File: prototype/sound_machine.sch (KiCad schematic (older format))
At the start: 18 parts, among them J1 Conn_01x04, J10 Conn_01x01, J11 Conn_01x01, J12 Conn_01x01, J13 Conn_01x15, J16 Conn_01x15, J2 Conn_01x15, J3 Conn_01x15, J4 Conn_01x08, J5 Audio-Jack-3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

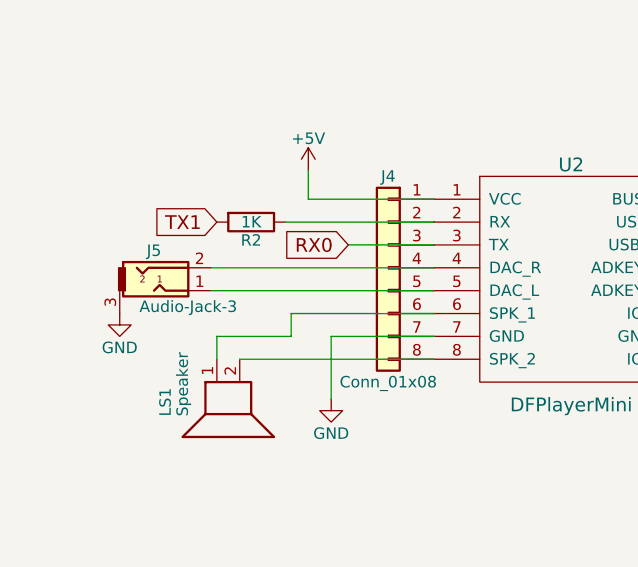
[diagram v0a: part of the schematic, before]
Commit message: Removed jack
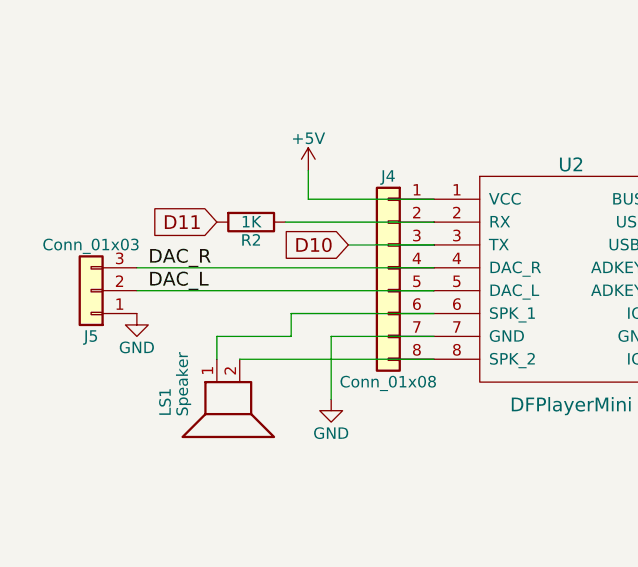
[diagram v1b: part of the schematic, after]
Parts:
- removed J5: Audio-Jack-3, Connectors:BARREL_JACK, symbol Audio-Jack-3
- added J5: Conn_01x03, Pin_Headers:Pin_Header_Straight_1x03_Pitch2.54mm, symbol Conn_01x03
- R1: footprint Resistors_SMD:R_0805_HandSoldering -> Resistors_THT:R_Axial_DIN0207_L6.3mm_D2.5mm_P10.16mm_Horizontal
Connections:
- net D10: now also J4.3 (Pin_3), U2.3 (TX)
- net D11: now also R2.2
- net GND: now also J5.1 (Pin_1)
- net RX0: no longer J4.3 (Pin_3), U2.3 (TX)
- net TX1: no longer R2.2
- net DAC_R: now reaches J4.4 (Pin_4), U2.4 (DAC_R)
- net DAC_R: now also J5.3 (Pin_3)
- net DAC_L: now reaches J4.5 (Pin_5), U2.5 (DAC_L)
- net DAC_L: now also J5.2 (Pin_2)
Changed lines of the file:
@@
 F 0 "R1" V 8430 2900 50  0000 C CNN
 F 1 "330R" V 8350 2900 50  0000 C CNN
-F 2 "Resistors_SMD:R_0805_HandSoldering" V 8280 2900 50  0001 C CNN
+F 2 "Resistors_THT:R_Axial_DIN0207_L6.3mm_D2.5mm_P10.16mm_Horizontal" V 8280 2900 50  0001 C CNN
 F 3 "" H 8350 2900 50  0001 C CNN
 	1    8350 2900
@@
 NoConn ~ 8500 2800
 $Comp
-L Audio-Jack-3 J5
-U 1 1 5A3D91A5
-P 2625 4575
-F 0 "J5" H 2575 4750 50  0000 C CNN
-F 1 "Audio-Jack-3" H 2725 4505 50  0000 C CNN
-F 2 "Connectors:BARREL_JACK" H 2875 4675 50  0001 C CNN
-F 3 "" H 2875 4675 50  0001 C CNN
-	1    2625 4575
-	1    0    0    -1
-$EndComp
-$Comp
 L GND #PWR010
 U 1 1 5A3D91F2
-P 2425 4675
-F 0 "#PWR010" H 2425 4425 50  0001 C CNN
-F 1 "GND" H 2425 4525 50  0000 C CNN
-F 2 "" H 2425 4675 50  0001 C CNN
-F 3 "" H 2425 4675 50  0001 C CNN
-	1    2425 4675
-	1    0    0    -1
-$EndComp
-Text GLabel 2850 4275 0    60   Input ~ 0
-TX1
-Text GLabel 3425 4375 0    60   Input ~ 0
-RX0
+P 2500 4675
+F 0 "#PWR010" H 2500 4425 50  0001 C CNN
+F 1 "GND" H 2500 4525 50  0000 C CNN
+F 2 "" H 2500 4675 50  0001 C CNN
+F 3 "" H 2500 4675 50  0001 C CNN
+	1    2500 4675
+	1    0    0    -1
+$EndComp
 $Comp
 L R R2
@@
 	2850 4775 2850 4875
 Wire Wire Line
-	2825 4575 3800 4575
-Wire Wire Line
-	2825 4475 3800 4475
+	2500 4575 3800 4575
+Wire Wire Line
+	2500 4475 3800 4475
 Wire Wire Line
 	3150 4275 3800 4275
@@
 	1    0    0    -1
 $EndComp
+Text GLabel 3425 4375 0    60   Input ~ 0
+D10
+Text GLabel 2850 4275 0    60   Input ~ 0
+D11
+$Comp
+L Conn_01x03 J5
+U 1 1 5A438329
+P 2300 4575
+F 0 "J5" H 2300 4775 50  0000 C CNN
+F 1 "Conn_01x03" H 2300 4375 50  0000 C CNN
+F 2 "Pin_Headers:Pin_Header_Straight_1x03_Pitch2.54mm" H 2300 4575 50  0001 C CNN
+F 3 "" H 2300 4575 50  0001 C CNN
+	1    2300 4575
+	-1   0    0    1
+$EndComp
+Text Label 2550 4475 0    60   ~ 0
+DAC_R
+Text Label 2550 4575 0    60   ~ 0
+DAC_L
 $EndSCHEMATC

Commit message: Capacitor
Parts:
- added C1: 10uf, Capacitors_THT:CP_Radial_D5.0mm_P2.50mm, symbol CP
- J1: footprint Pin_Headers:Pin_Header_Straight_1x04_Pitch2.54mm -> Socket_Strips:Socket_Strip_Straight_1x04
- J13, J16: footprint Pin_Headers:Pin_Header_Straight_1x15_Pitch2.54mm -> Socket_Strips:Socket_Strip_Straight_1x15_Pitch2.54mm
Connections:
- net +5V: now also C1.1
- net GND: now also C1.2
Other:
- moved on the sheet: J16, J3
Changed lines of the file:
@@
 L Conn_01x15 J3
 U 1 1 5A3D80E6
-P 4275 2350
-F 0 "J3" H 4275 3150 50  0000 C CNN
-F 1 "Conn_01x15" H 4275 1550 50  0000 C CNN
-F 2 "Pin_Headers:Pin_Header_Straight_1x15_Pitch2.54mm" H 4275 2350 50  0001 C CNN
-F 3 "" H 4275 2350 50  0001 C CNN
-	1    4275 2350
+P 5425 2375
+F 0 "J3" H 5425 3175 50  0000 C CNN
+F 1 "Conn_01x15" H 5425 1575 50  0000 C CNN
+F 2 "Pin_Headers:Pin_Header_Straight_1x15_Pitch2.54mm" H 5425 2375 50  0001 C CNN
+F 3 "" H 5425 2375 50  0001 C CNN
+	1    5425 2375
 	-1   0    0    -1
 $EndComp
-Text GLabel 4475 1650 2    60   Input ~ 0
+Text GLabel 5625 1675 2    60   Input ~ 0
 VIN
-Text GLabel 4475 1850 2    60   Input ~ 0
+Text GLabel 5625 1875 2    60   Input ~ 0
 RESET
-Text GLabel 4475 2050 2    60   Input ~ 0
+Text GLabel 5625 2075 2    60   Input ~ 0
 A7
-Text GLabel 4475 2150 2    60   Input ~ 0
+Text GLabel 5625 2175 2    60   Input ~ 0
 A6
-Text GLabel 4475 2450 2    60   Input ~ 0
+Text GLabel 5625 2475 2    60   Input ~ 0
 A3
-Text GLabel 4475 2550 2    60   Input ~ 0
+Text GLabel 5625 2575 2    60   Input ~ 0
 A2
-Text GLabel 4475 2650 2    60   Input ~ 0
+Text GLabel 5625 2675 2    60   Input ~ 0
 A1
-Text GLabel 4475 2750 2    60   Input ~ 0
+Text GLabel 5625 2775 2    60   Input ~ 0
 A0
-Text GLabel 4475 2850 2    60   Input ~ 0
+Text GLabel 5625 2875 2    60   Input ~ 0
 AHREF
-Text GLabel 4475 3050 2    60   Input ~ 0
+Text GLabel 5625 3075 2    60   Input ~ 0
 D13
 $Comp
 L +3.3V #PWR07
 U 1 1 5A3D8305
-P 5025 2950
-F 0 "#PWR07" H 5025 2800 50  0001 C CNN
-F 1 "+3.3V" H 5025 3090 50  0000 C CNN
-F 2 "" H 5025 2950 50  0001 C CNN
-F 3 "" H 5025 2950 50  0001 C CNN
-	1    5025 2950
+P 6175 2975
+F 0 "#PWR07" H 6175 2825 50  0001 C CNN
+F 1 "+3.3V" H 6175 3115 50  0000 C CNN
+F 2 "" H 6175 2975 50  0001 C CNN
+F 3 "" H 6175 2975 50  0001 C CNN
+	1    6175 2975
 	1    0    0    -1
 $EndComp
@@
 L +5V #PWR08
 U 1 1 5A3D8374
-P 5000 1950
-F 0 "#PWR08" H 5000 1800 50  0001 C CNN
-F 1 "+5V" H 5000 2090 50  0000 C CNN
-F 2 "" H 5000 1950 50  0001 C CNN
-F 3 "" H 5000 1950 50  0001 C CNN
-	1    5000 1950
+P 6150 1975
+F 0 "#PWR08" H 6150 1825 50  0001 C CNN
+F 1 "+5V" H 6150 2115 50  0000 C CNN
+F 2 "" H 6150 1975 50  0001 C CNN
+F 3 "" H 6150 1975 50  0001 C CNN
+	1    6150 1975
 	1    0    0    -1
 $EndComp
@@
 L GND #PWR09
 U 1 1 5A3D83F0
-P 5200 1750
-F 0 "#PWR09" H 5200 1500 50  0001 C CNN
-F 1 "GND" H 5200 1600 50  0000 C CNN
-F 2 "" H 5200 1750 50  0001 C CNN
-F 3 "" H 5200 1750 50  0001 C CNN
-	1    5200 1750
-	1    0    0    -1
-$EndComp
-Text GLabel 4475 2250 2    60   Input ~ 0
+P 6350 1775
+F 0 "#PWR09" H 6350 1525 50  0001 C CNN
+F 1 "GND" H 6350 1625 50  0000 C CNN
+F 2 "" H 6350 1775 50  0001 C CNN
+F 3 "" H 6350 1775 50  0001 C CNN
+	1    6350 1775
+	1    0    0    -1
+$EndComp
+Text GLabel 5625 2275 2    60   Input ~ 0
 SCL
-Text GLabel 4475 2350 2    60   Input ~ 0
+Text GLabel 5625 2375 2    60   Input ~ 0
 SDA
 Text GLabel 8200 2900 0    60   Input ~ 0
@@
 	2075 1975 2425 1975
 Wire Wire Line
-	5025 2950 4475 2950
-Wire Wire Line
-	5000 1950 4475 1950
-Wire Wire Line
-	4475 1750 5200 1750
+	6175 2975 5625 2975
+Wire Wire Line
+	6150 1975 5625 1975
+Wire Wire Line
+	5625 1775 6350 1775
 Wire Wire Line
 	2950 4875 3800 4875
@@
 F 0 "J13" H 3375 3175 50  0000 C CNN
 F 1 "Conn_01x15" H 3375 1575 50  0000 C CNN
-F 2 "Pin_Headers:Pin_Header_Straight_1x15_Pitch2.54mm" H 3375 2375 50  0001 C CNN
+F 2 "Socket_Strips:Socket_Strip_Straight_1x15_Pitch2.54mm" H 3375 2375 50  0001 C CNN
 F 3 "" H 3375 2375 50  0001 C CNN
 	1    3375 2375
@@
 L Conn_01x15 J16
 U 1 1 5A3DC180
-P 5400 2350
-F 0 "J16" H 5400 3150 50  0000 C CNN
-F 1 "Conn_01x15" H 5400 1550 50  0000 C CNN
-F 2 "Pin_Headers:Pin_Header_Straight_1x15_Pitch2.54mm" H 5400 2350 50  0001 C CNN
-F 3 "" H 5400 2350 50  0001 C CNN
-	1    5400 2350
+P 4250 2375
+F 0 "J16" H 4250 3175 50  0000 C CNN
+F 1 "Conn_01x15" H 4250 1575 50  0000 C CNN
+F 2 "Socket_Strips:Socket_Strip_Straight_1x15_Pitch2.54mm" H 4250 2375 50  0001 C CNN
+F 3 "" H 4250 2375 50  0001 C CNN
+	1    4250 2375
 	-1   0    0    -1
 $EndComp
-Text GLabel 5600 1650 2    60   Input ~ 0
+Text GLabel 4450 1675 2    60   Input ~ 0
 VIN
-Text GLabel 5600 1850 2    60   Input ~ 0
+Text GLabel 4450 1875 2    60   Input ~ 0
 RESET
-Text GLabel 5600 2050 2    60   Input ~ 0
+Text GLabel 4450 2075 2    60   Input ~ 0
 A7
-Text GLabel 5600 2150 2    60   Input ~ 0
+Text GLabel 4450 2175 2    60   Input ~ 0
 A6
-Text GLabel 5600 2450 2    60   Input ~ 0
+Text GLabel 4450 2475 2    60   Input ~ 0
 A3
-Text GLabel 5600 2550 2    60   Input ~ 0
+Text GLabel 4450 2575 2    60   Input ~ 0
 A2
-Text GLabel 5600 2650 2    60   Input ~ 0
+Text GLabel 4450 2675 2    60   Input ~ 0
 A1
-Text GLabel 5600 2750 2    60   Input ~ 0
+Text GLabel 4450 2775 2    60   Input ~ 0
 A0
-Text GLabel 5600 2850 2    60   Input ~ 0
+Text GLabel 4450 2875 2    60   Input ~ 0
 AHREF
-Text GLabel 5600 3050 2    60   Input ~ 0
+Text GLabel 4450 3075 2    60   Input ~ 0
 D13
 $Comp
 L +3.3V #PWR017
 U 1 1 5A3DC190
-P 6150 2950
-F 0 "#PWR017" H 6150 2800 50  0001 C CNN
-F 1 "+3.3V" H 6150 3090 50  0000 C CNN
-F 2 "" H 6150 2950 50  0001 C CNN
-F 3 "" H 6150 2950 50  0001 C CNN
-	1    6150 2950
+P 5000 2975
+F 0 "#PWR017" H 5000 2825 50  0001 C CNN
+F 1 "+3.3V" H 5000 3115 50  0000 C CNN
+F 2 "" H 5000 2975 50  0001 C CNN
+F 3 "" H 5000 2975 50  0001 C CNN
+	1    5000 2975
 	1    0    0    -1
 $EndComp
@@
 L +5V #PWR018
 U 1 1 5A3DC196
-P 6125 1950
-F 0 "#PWR018" H 6125 1800 50  0001 C CNN
-F 1 "+5V" H 6125 2090 50  0000 C CNN
-F 2 "" H 6125 1950 50  0001 C CNN
-F 3 "" H 6125 1950 50  0001 C CNN
-	1    6125 1950
+P 4975 1975
+F 0 "#PWR018" H 4975 1825 50  0001 C CNN
+F 1 "+5V" H 4975 2115 50  0000 C CNN
+F 2 "" H 4975 1975 50  0001 C CNN
+F 3 "" H 4975 1975 50  0001 C CNN
+	1    4975 1975
 	1    0    0    -1
 $EndComp
@@
 L GND #PWR019
 U 1 1 5A3DC19C
-P 6325 1750
-F 0 "#PWR019" H 6325 1500 50  0001 C CNN
-F 1 "GND" H 6325 1600 50  0000 C CNN
-F 2 "" H 6325 1750 50  0001 C CNN
-F 3 "" H 6325 1750 50  0001 C CNN
-	1    6325 1750
-	1    0    0    -1
-$EndComp
-Text GLabel 5600 2250 2    60   Input ~ 0
+P 5175 1775
+F 0 "#PWR019" H 5175 1525 50  0001 C CNN
+F 1 "GND" H 5175 1625 50  0000 C CNN
+F 2 "" H 5175 1775 50  0001 C CNN
+F 3 "" H 5175 1775 50  0001 C CNN
+	1    5175 1775
+	1    0    0    -1
+$EndComp
+Text GLabel 4450 2275 2    60   Input ~ 0
 SCL
-Text GLabel 5600 2350 2    60   Input ~ 0
+Text GLabel 4450 2375 2    60   Input ~ 0
 SDA
 Wire Wire Line
-	6150 2950 5600 2950
-Wire Wire Line
-	6125 1950 5600 1950
-Wire Wire Line
-	5600 1750 6325 1750
+	5000 2975 4450 2975
+Wire Wire Line
+	4975 1975 4450 1975
+Wire Wire Line
+	4450 1775 5175 1775
 $Comp
 L Conn_01x08 J6
@@
 F 0 "J1" H 9175 5400 50  0000 C CNN
 F 1 "Conn_01x04" H 9175 4900 50  0000 C CNN
-F 2 "Pin_Headers:Pin_Header_Straight_1x04_Pitch2.54mm" H 9175 5200 50  0001 C CNN
+F 2 "Socket_Strips:Socket_Strip_Straight_1x04" H 9175 5200 50  0001 C CNN
 F 3 "" H 9175 5200 50  0001 C CNN
 	1    9175 5200
@@
 Text Label 2550 4575 0    60   ~ 0
 DAC_L
+$Comp
+L CP C1
+U 1 1 5A43926F
+P 8250 4450
+F 0 "C1" H 8275 4550 50  0000 L CNN
+F 1 "10uf" H 8275 4350 50  0000 L CNN
+F 2 "Capacitors_THT:CP_Radial_D5.0mm_P2.50mm" H 8288 4300 50  0001 C CNN
+F 3 "" H 8250 4450 50  0001 C CNN
+	1    8250 4450
+	1    0    0    -1
+$EndComp
+$Comp
+L GND #PWR022
+U 1 1 5A43932F
+P 8250 4600
+F 0 "#PWR022" H 8250 4350 50  0001 C CNN
+F 1 "GND" H 8250 4450 50  0000 C CNN
+F 2 "" H 8250 4600 50  0001 C CNN
+F 3 "" H 8250 4600 50  0001 C CNN
+	1    8250 4600
+	1    0    0    -1
+$EndComp
+$Comp
+L +5V #PWR023
+U 1 1 5A439399
+P 8250 4300
+F 0 "#PWR023" H 8250 4150 50  0001 C CNN
+F 1 "+5V" H 8250 4440 50  0000 C CNN
+F 2 "" H 8250 4300 50  0001 C CNN
+F 3 "" H 8250 4300 50  0001 C CNN
+	1    8250 4300
+	1    0    0    -1
+$EndComp
 $EndSCHEMATC
